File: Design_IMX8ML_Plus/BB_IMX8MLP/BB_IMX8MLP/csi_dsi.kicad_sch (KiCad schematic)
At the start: 0 parts

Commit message: improving the usb conector
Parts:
- added J12: DSI, symbol Connector:Conn_01x34_Pin
- added J13: CSI, symbol Connector:Conn_01x26_Pin

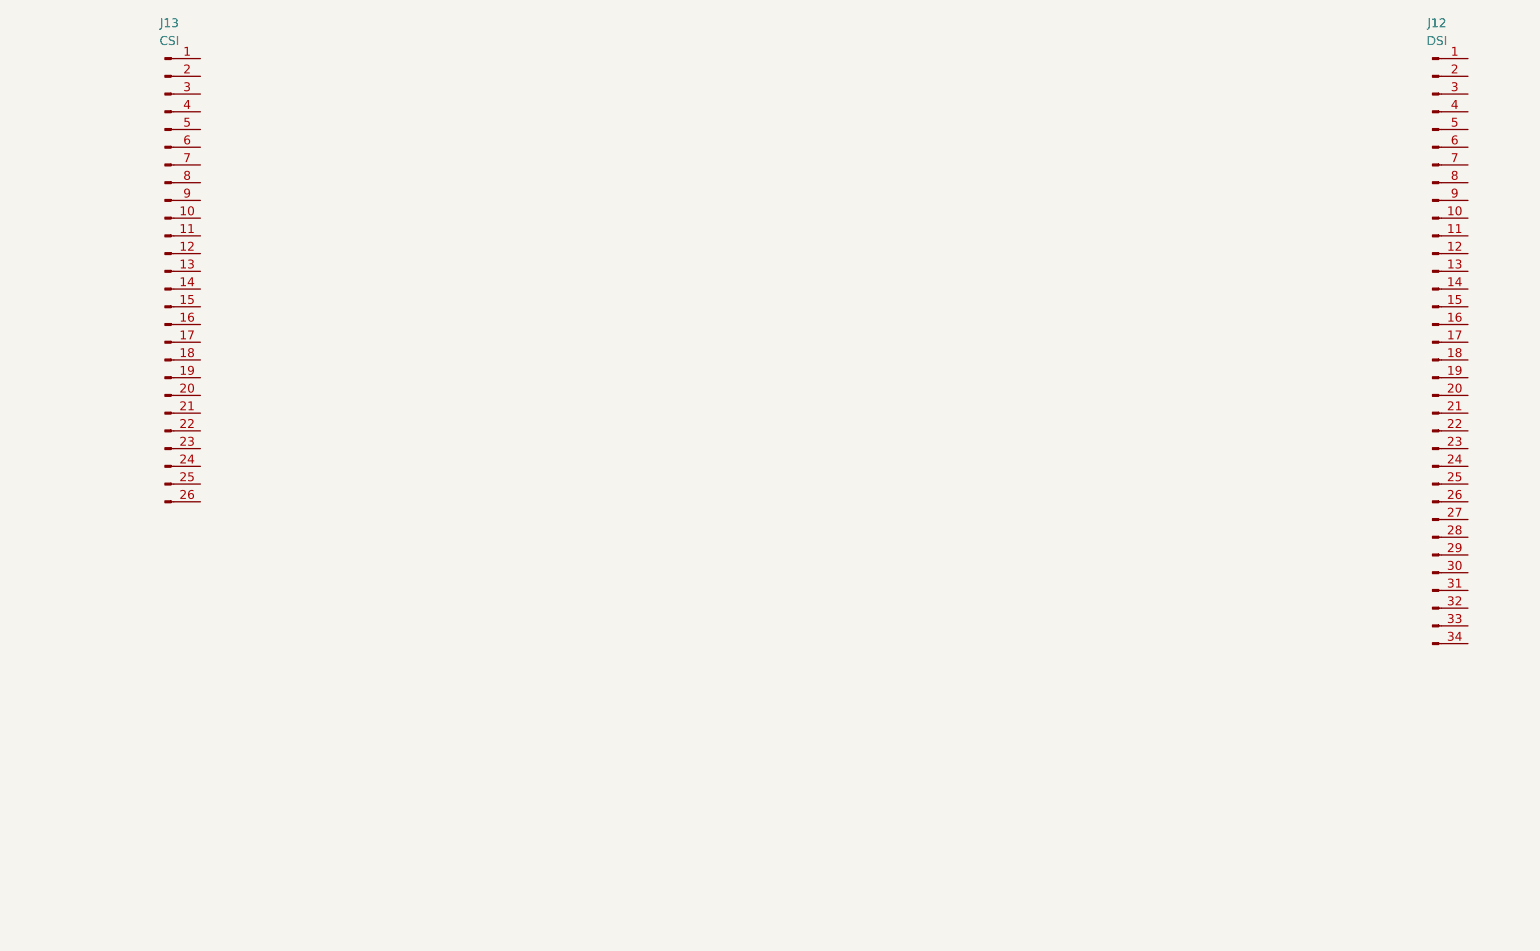
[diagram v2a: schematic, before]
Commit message: improving Ethernet, USB and Camera inteface
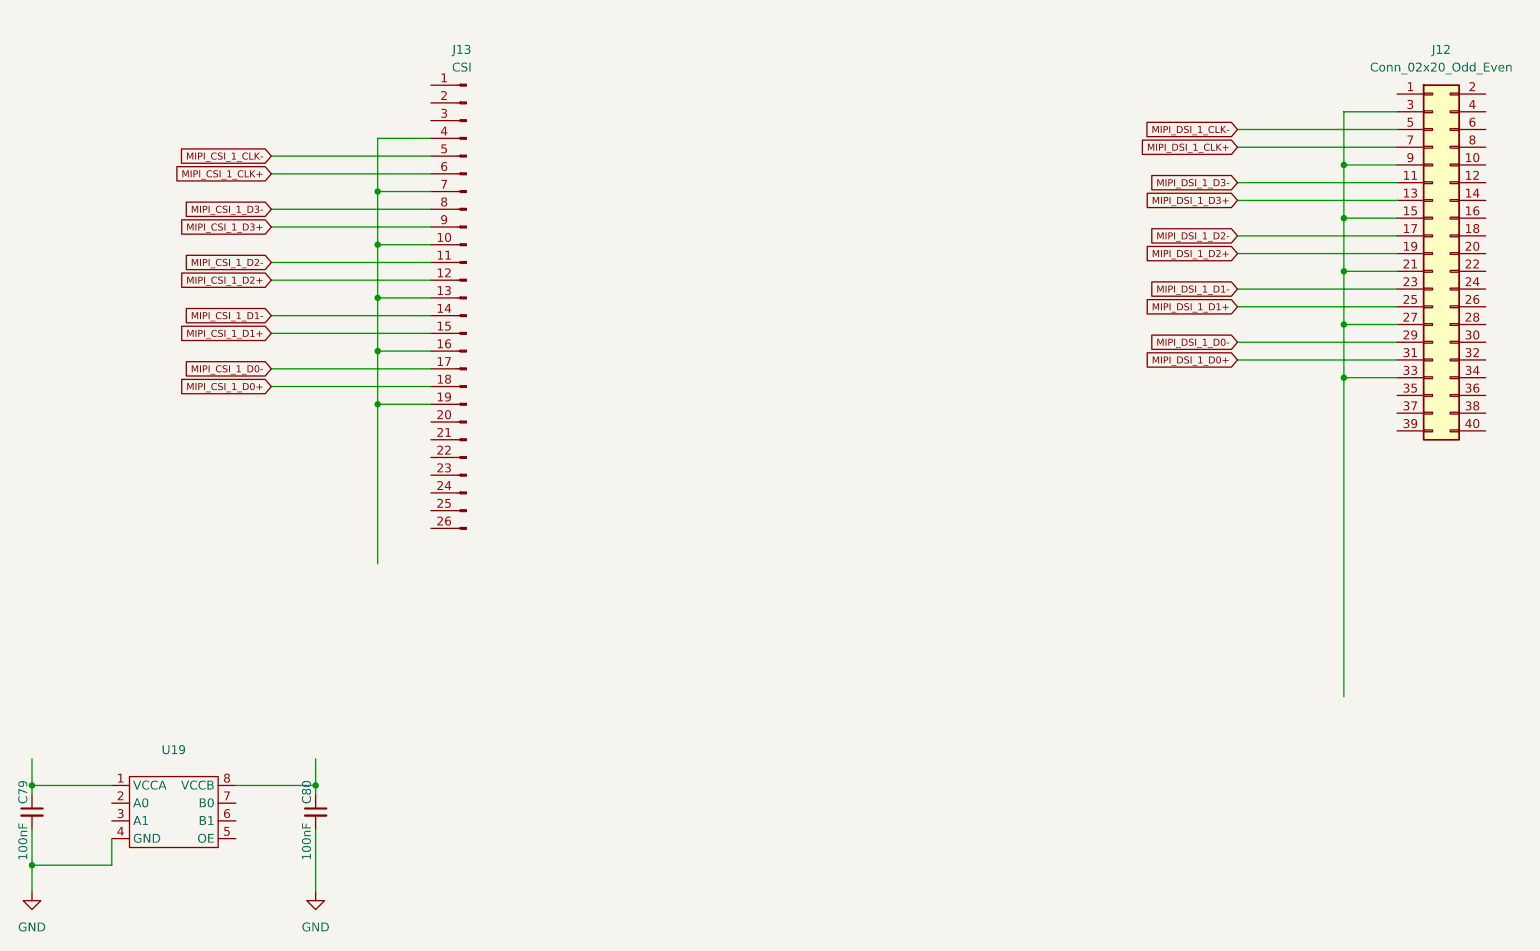
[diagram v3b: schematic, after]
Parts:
- removed J12: DSI, symbol Connector:Conn_01x34_Pin
- added C79, C80: 100nF, Capacitor_SMD:C_0402_1005Metric, symbol Device:C_Small
- added J12: Conn_02x20_Odd_Even, symbol Connector_Generic:Conn_02x20_Odd_Even
- added U19: ~, _W_SBC:MICROPAK8_1P6X1P6_ONS, symbol _W_MX8M:FXMA2102L8X
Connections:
- net at J13.10 (Pin_10): now also J13.13 (Pin_13), J13.16 (Pin_16), J13.19 (Pin_19), J13.4 (Pin_4), J13.7 (Pin_7)
- net MIPI_CSI_1_D2-: now reaches J13.11 (Pin_11)
- net MIPI_CSI_1_D2+: now reaches J13.12 (Pin_12)
- net MIPI_CSI_1_D1-: now reaches J13.14 (Pin_14)
- net MIPI_CSI_1_D1+: now reaches J13.15 (Pin_15)
- net MIPI_CSI_1_D0-: now reaches J13.17 (Pin_17)
- net MIPI_CSI_1_D0+: now reaches J13.18 (Pin_18)
- net MIPI_CSI_1_CLK-: now reaches J13.5 (Pin_5)
- net MIPI_CSI_1_CLK+: now reaches J13.6 (Pin_6)
- net MIPI_CSI_1_D3-: now reaches J13.8 (Pin_8)
- net MIPI_CSI_1_D3+: now reaches J13.9 (Pin_9)
- new net: C80.1, U19.8 (VCCB)
- new net: C79.1, U19.1 (VCCA)
- new net: J12.15 (Pin_15), J12.21 (Pin_21), J12.27 (Pin_27), J12.3 (Pin_3), J12.33 (Pin_33), J12.9 (Pin_9)
- new net GND: C79.2, C80.2, U19.4 (GND)
- new net MIPI_DSI_1_CLK+: J12.7 (Pin_7)
- new net MIPI_DSI_1_CLK-: J12.5 (Pin_5)
- new net MIPI_DSI_1_D0+: J12.31 (Pin_31)
- new net MIPI_DSI_1_D0-: J12.29 (Pin_29)
- new net MIPI_DSI_1_D1+: J12.25 (Pin_25)
- new net MIPI_DSI_1_D1-: J12.23 (Pin_23)
- new net MIPI_DSI_1_D2+: J12.19 (Pin_19)
- new net MIPI_DSI_1_D2-: J12.17 (Pin_17)
- new net MIPI_DSI_1_D3+: J12.13 (Pin_13)
- new net MIPI_DSI_1_D3-: J12.11 (Pin_11)
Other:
- moved on the sheet: J13

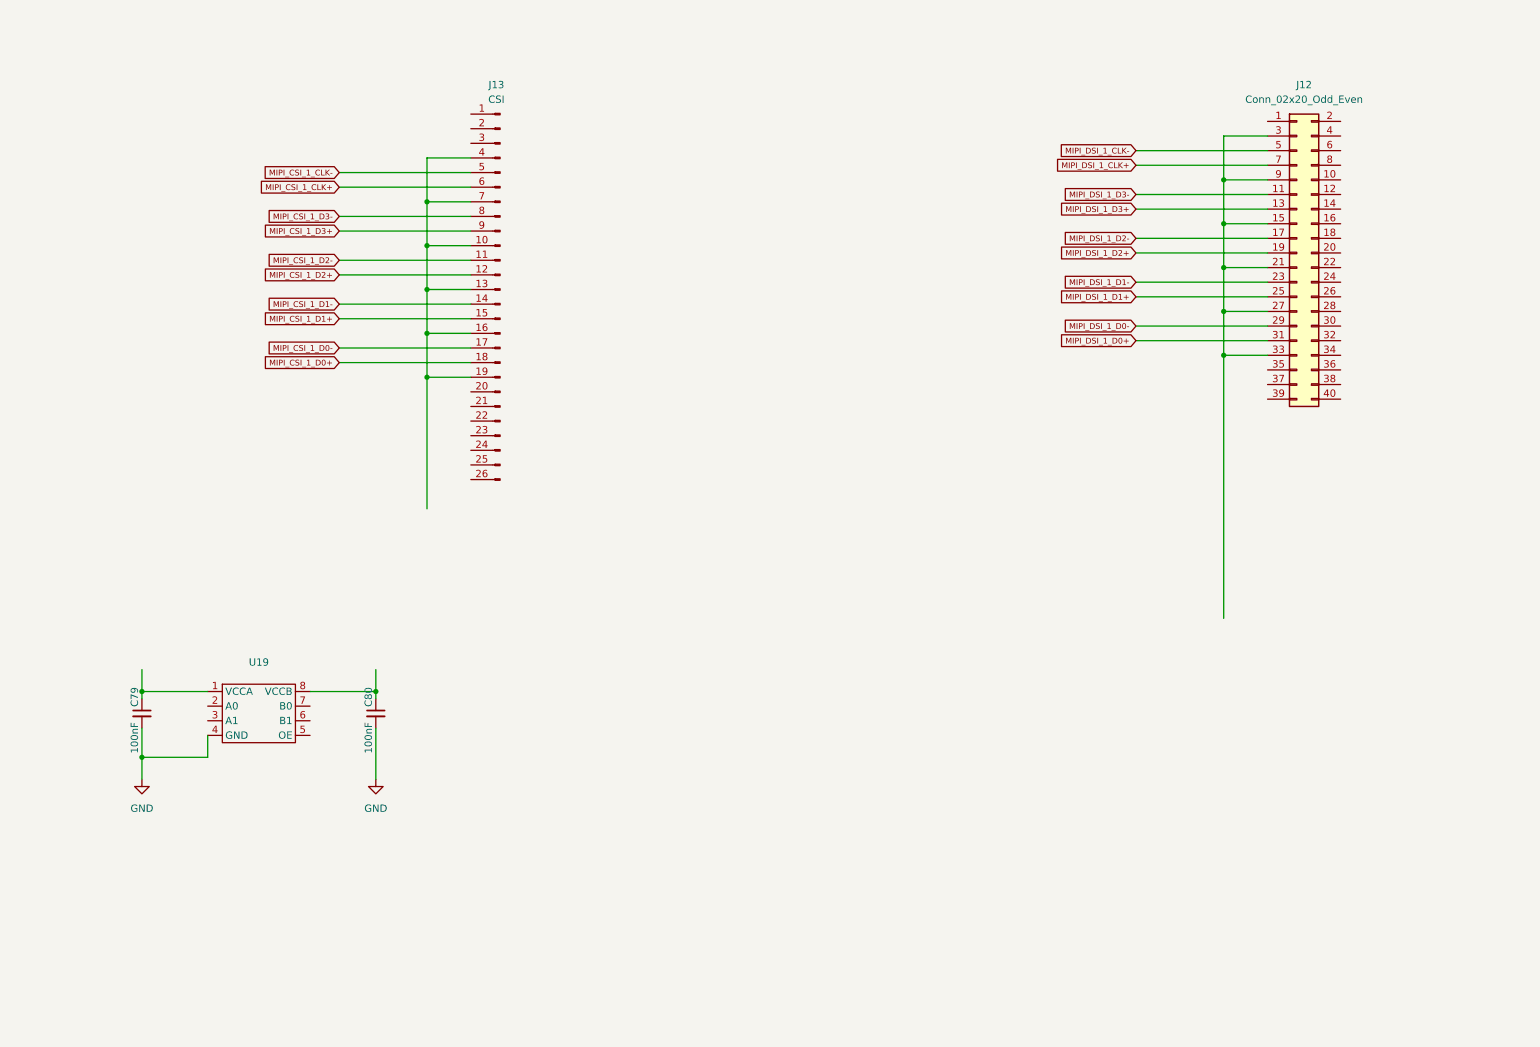
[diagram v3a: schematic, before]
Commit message: Add LVDs and CSI Interface
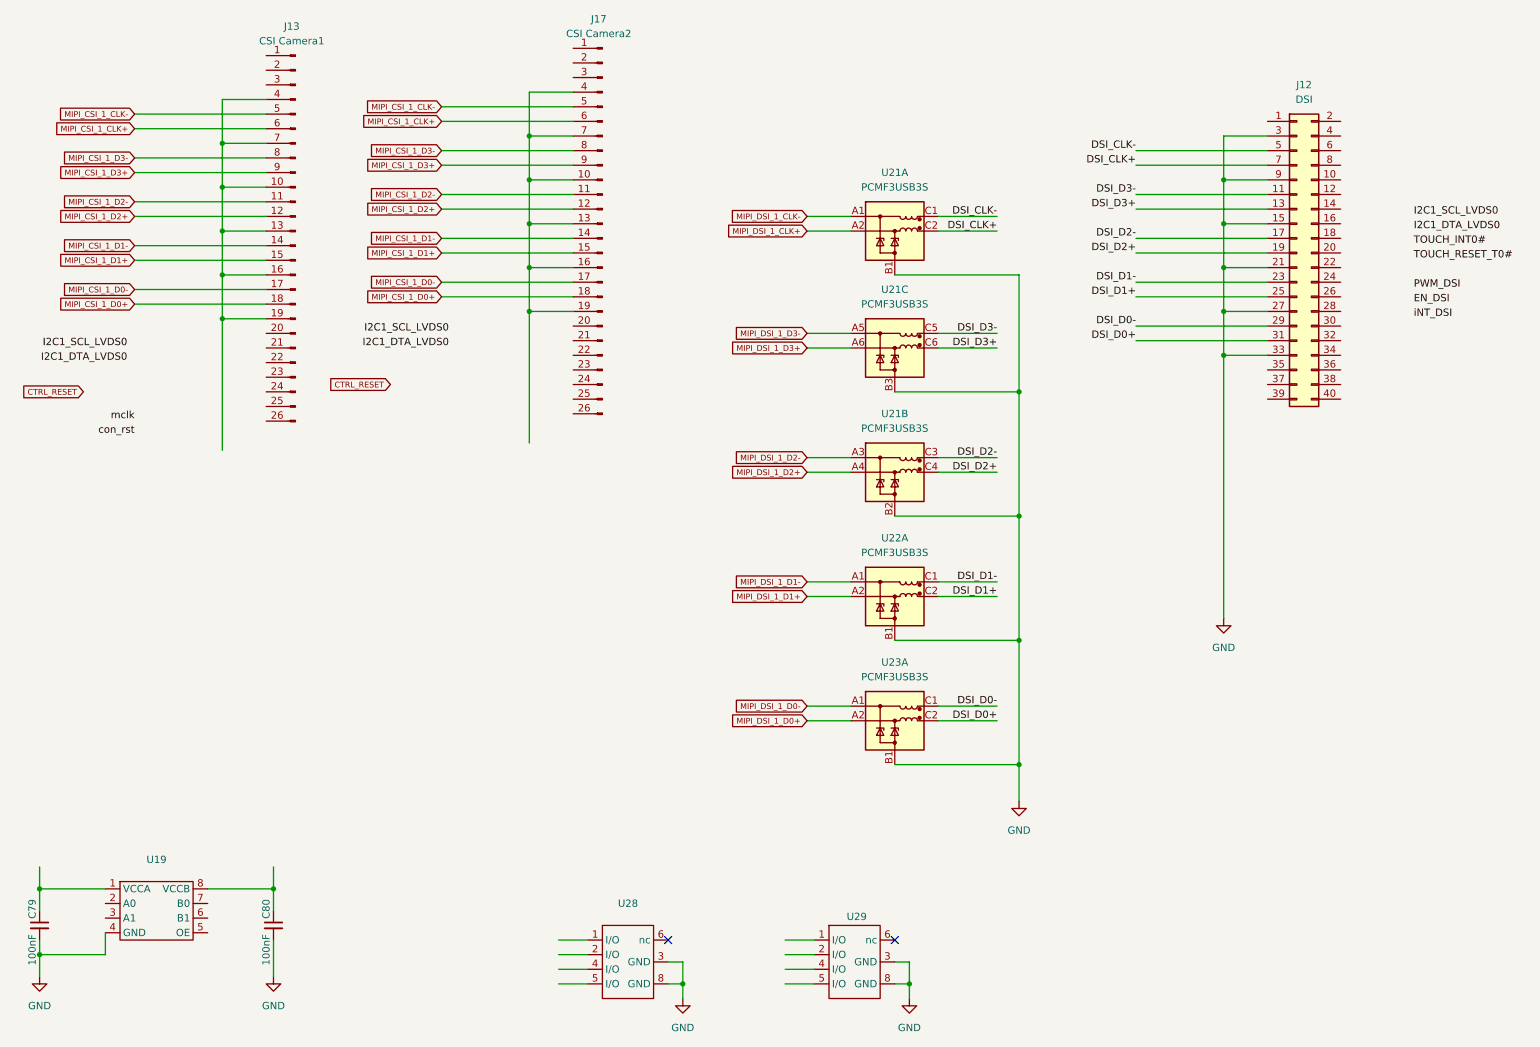
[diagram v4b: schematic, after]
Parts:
- added J17: CSI Camera2, symbol Connector:Conn_01x26_Pin
- added U21, U22, U23: PCMF3USB3S, Package_CSP:Nexperia_WLCSP-15_6-3-6_2.37x1.17mm_Layout6x3_P0.4mm, symbol Power_Protection:PCMF3USB3S
- added U28, U29: ~, _W_SBC:DFN10_U-DFN2510-10_DIO, symbol _W_MX8M:D3V3F4U10LP-7
- J12: value Conn_02x20_Odd_Even -> DSI
- J13: value CSI -> CSI Camera1
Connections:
- net GND: now also J12.15 (Pin_15), J12.21 (Pin_21), J12.27 (Pin_27), J12.3 (Pin_3), J12.33 (Pin_33), J12.9 (Pin_9), U21.B1 (GND_CH1), U21.B2 (GND_CH2), U21.B3 (GND_CH3), U22.B1 (GND_CH1), U23.B1 (GND_CH1), U28.3 (GND), U28.8 (GND), U29.3 (GND), U29.8 (GND)
- net MIPI_CSI_1_CLK+: now also J17.6 (Pin_6)
- net MIPI_CSI_1_CLK-: now also J17.5 (Pin_5)
- net MIPI_CSI_1_D0+: now also J17.18 (Pin_18)
- net MIPI_CSI_1_D0-: now also J17.17 (Pin_17)
- net MIPI_CSI_1_D1+: now also J17.15 (Pin_15)
- net MIPI_CSI_1_D1-: now also J17.14 (Pin_14)
- net MIPI_CSI_1_D2+: now also J17.12 (Pin_12)
- net MIPI_CSI_1_D2-: now also J17.11 (Pin_11)
- net MIPI_CSI_1_D3+: now also J17.9 (Pin_9)
- net MIPI_CSI_1_D3-: now also J17.8 (Pin_8)
- net MIPI_DSI_1_CLK+: now also U21.A2 (CH1_IN-); no longer J12.7 (Pin_7)
- net MIPI_DSI_1_CLK-: now also U21.A1 (CH1_IN+); no longer J12.5 (Pin_5)
- net MIPI_DSI_1_D0+: now also U23.A2 (CH1_IN-); no longer J12.31 (Pin_31)
- net MIPI_DSI_1_D0-: now also U23.A1 (CH1_IN+); no longer J12.29 (Pin_29)
- net MIPI_DSI_1_D1+: now also U22.A2 (CH1_IN-); no longer J12.25 (Pin_25)
- net MIPI_DSI_1_D1-: now also U22.A1 (CH1_IN+); no longer J12.23 (Pin_23)
- net MIPI_DSI_1_D2+: now also U21.A4 (CH2_IN-); no longer J12.19 (Pin_19)
- net MIPI_DSI_1_D2-: now also U21.A3 (CH2_IN+); no longer J12.17 (Pin_17)
- net MIPI_DSI_1_D3+: now also U21.A6 (CH3_IN-); no longer J12.13 (Pin_13)
- net MIPI_DSI_1_D3-: now also U21.A5 (CH3_IN+); no longer J12.11 (Pin_11)
- new net: U29.10 (nc), U29.6 (nc), U29.7 (nc), U29.9 (nc)
- new net: J17.10 (Pin_10), J17.13 (Pin_13), J17.16 (Pin_16), J17.19 (Pin_19), J17.4 (Pin_4), J17.7 (Pin_7)
- new net: U28.10 (nc), U28.6 (nc), U28.7 (nc), U28.9 (nc)
- new net DSI_CLK+: J12.7 (Pin_7), U21.C2 (CH1_OUT-)
- new net DSI_CLK-: J12.5 (Pin_5), U21.C1 (CH1_OUT+)
- new net DSI_D0+: J12.31 (Pin_31), U23.C2 (CH1_OUT-)
- new net DSI_D0-: J12.29 (Pin_29), U23.C1 (CH1_OUT+)
- new net DSI_D1+: J12.25 (Pin_25), U22.C2 (CH1_OUT-)
- new net DSI_D1-: J12.23 (Pin_23), U22.C1 (CH1_OUT+)
- new net DSI_D2+: J12.19 (Pin_19), U21.C4 (CH2_OUT-)
- new net DSI_D2-: J12.17 (Pin_17), U21.C3 (CH2_OUT+)
- new net DSI_D3+: J12.13 (Pin_13), U21.C6 (CH3_OUT-)
- new net DSI_D3-: J12.11 (Pin_11), U21.C5 (CH3_OUT+)
- no-connect marks 0 -> 2
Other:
- moved on the sheet: C79, C80, J13, U19

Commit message: Review
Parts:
- added R64, R65, R66, R67: 10K, Resistor_SMD:R_0402_1005Metric, symbol Device:R_Small
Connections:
- net CTRL_RESET: now also J13.22 (Pin_22), J17.22 (Pin_22)
- net I2C1_DTA_LVDS0: now also J13.21 (Pin_21), J17.21 (Pin_21), U19.6 (B1), R65.2
- net I2C1_SCL_LVDS0: now also J13.20 (Pin_20), J17.20 (Pin_20), U19.7 (B0), R64.2
- net con_rst: now also J13.24 (Pin_24), J17.24 (Pin_24)
- net mclk: now also J13.23 (Pin_23), J17.23 (Pin_23)
- net 3v3: now reaches C80.1, U19.8 (VCCB)
- net 3v3: now also R64.1, R65.1
- net 1v8: now reaches C79.1, U19.1 (VCCA)
- net 1v8: now also R66.1, R67.1
- net I2C1_SCL: now reaches U19.2 (A0)
- net I2C1_SCL: now also R66.2
- net I2C1_SDA: now reaches U19.3 (A1)
- net I2C1_SDA: now also R67.2
